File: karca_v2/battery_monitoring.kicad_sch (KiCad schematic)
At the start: 15 parts, among them U34 INA180A2, U36 TLV9301xDBV, U41 NUP4202, U42 MCP3204

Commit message: discrete traces
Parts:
- renumbered C59 to C73, C60 to C74, C61 to C75, C70 to C76, C71 to C77, R112 to R116, R113 to R117, R114 to R118, R115 to R119, U34 to U43, U42 to U44, U41 to U45, U36 to U46

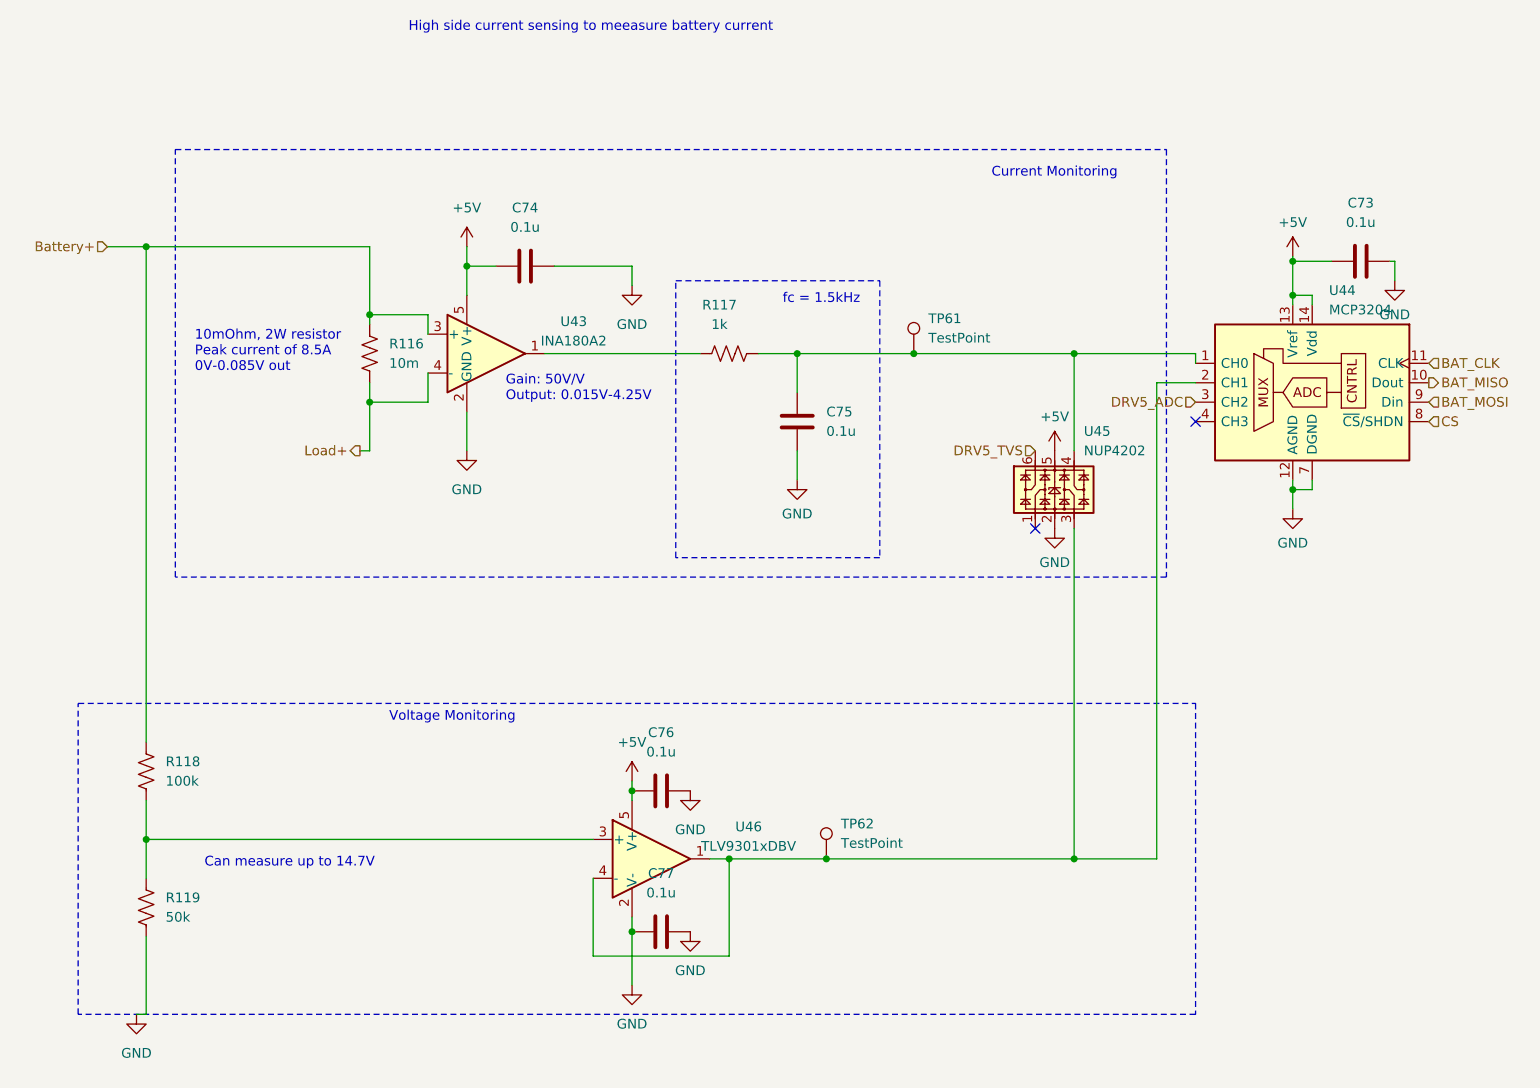
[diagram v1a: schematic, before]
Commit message: fixed TVS Diodes
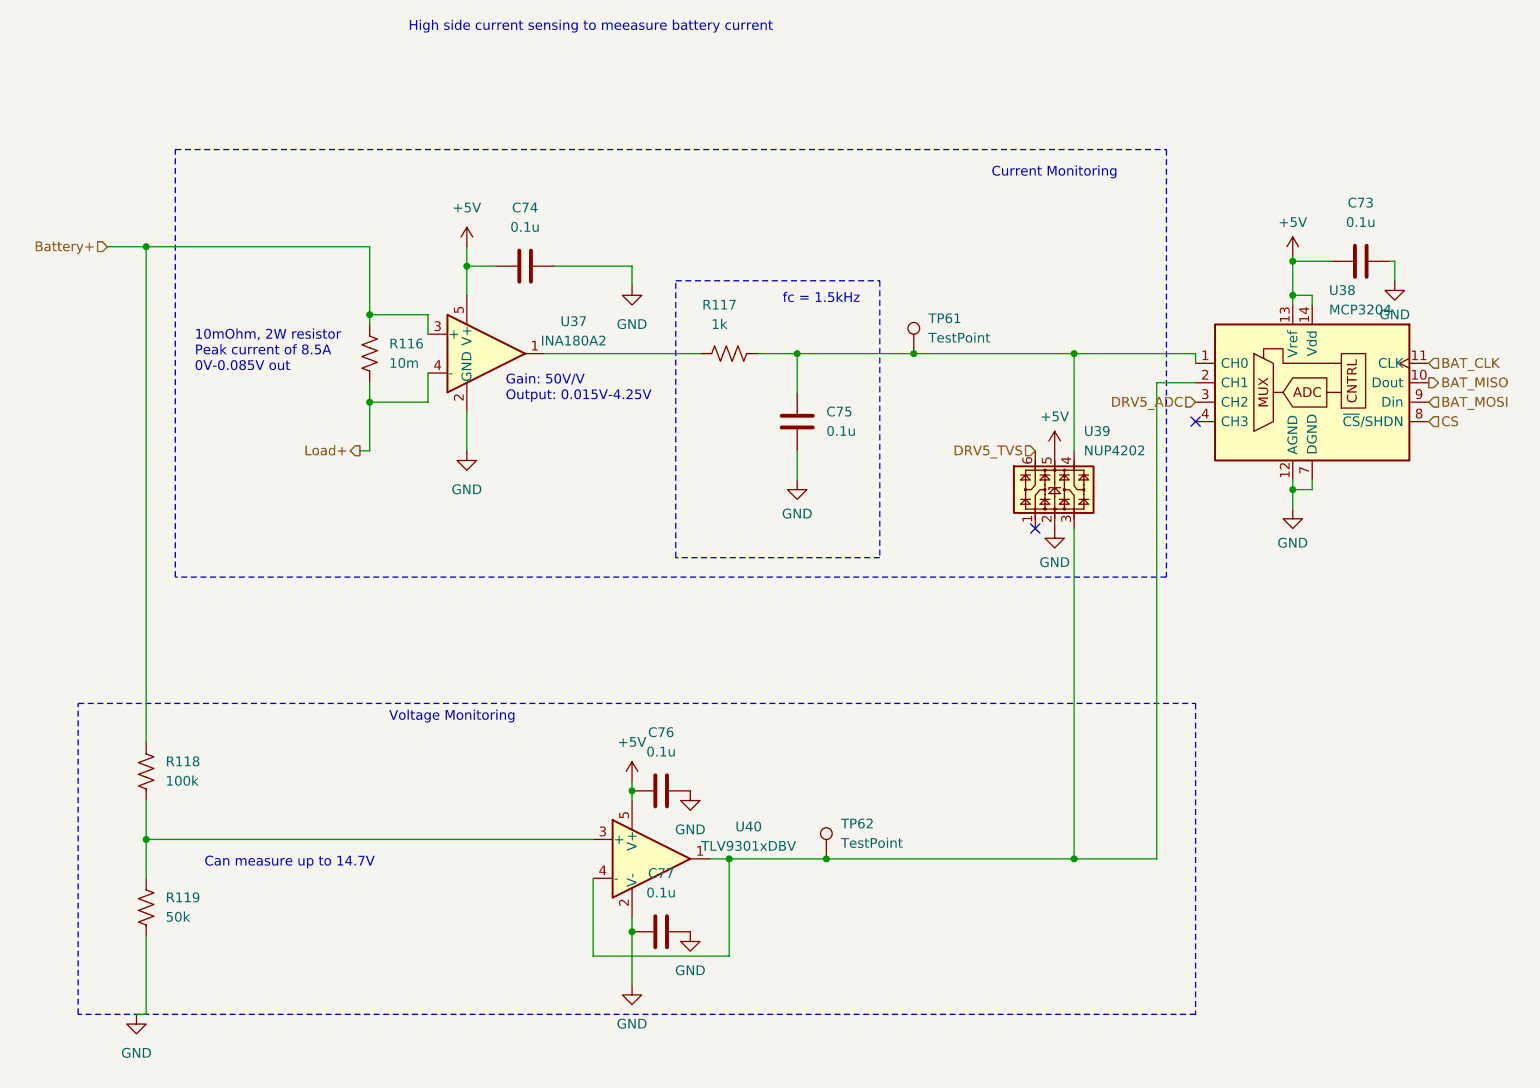
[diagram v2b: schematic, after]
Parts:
- renumbered U43 to U37, U44 to U38, U45 to U39, U46 to U40

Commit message: fixed violations
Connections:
- net BAT_CUR: now reaches C75.2, R117.2, TP61.1, U38.1 (CH0), U39.4
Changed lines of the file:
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@@
+    (effects (font (size 1.27 1.27)) (justify left bottom))
+  )
+  (label "BAT_CUR" (at 163.195 59.69 0) (fields_autoplaced)
     (effects (font (size 1.27 1.27)) (justify left bottom))
   )

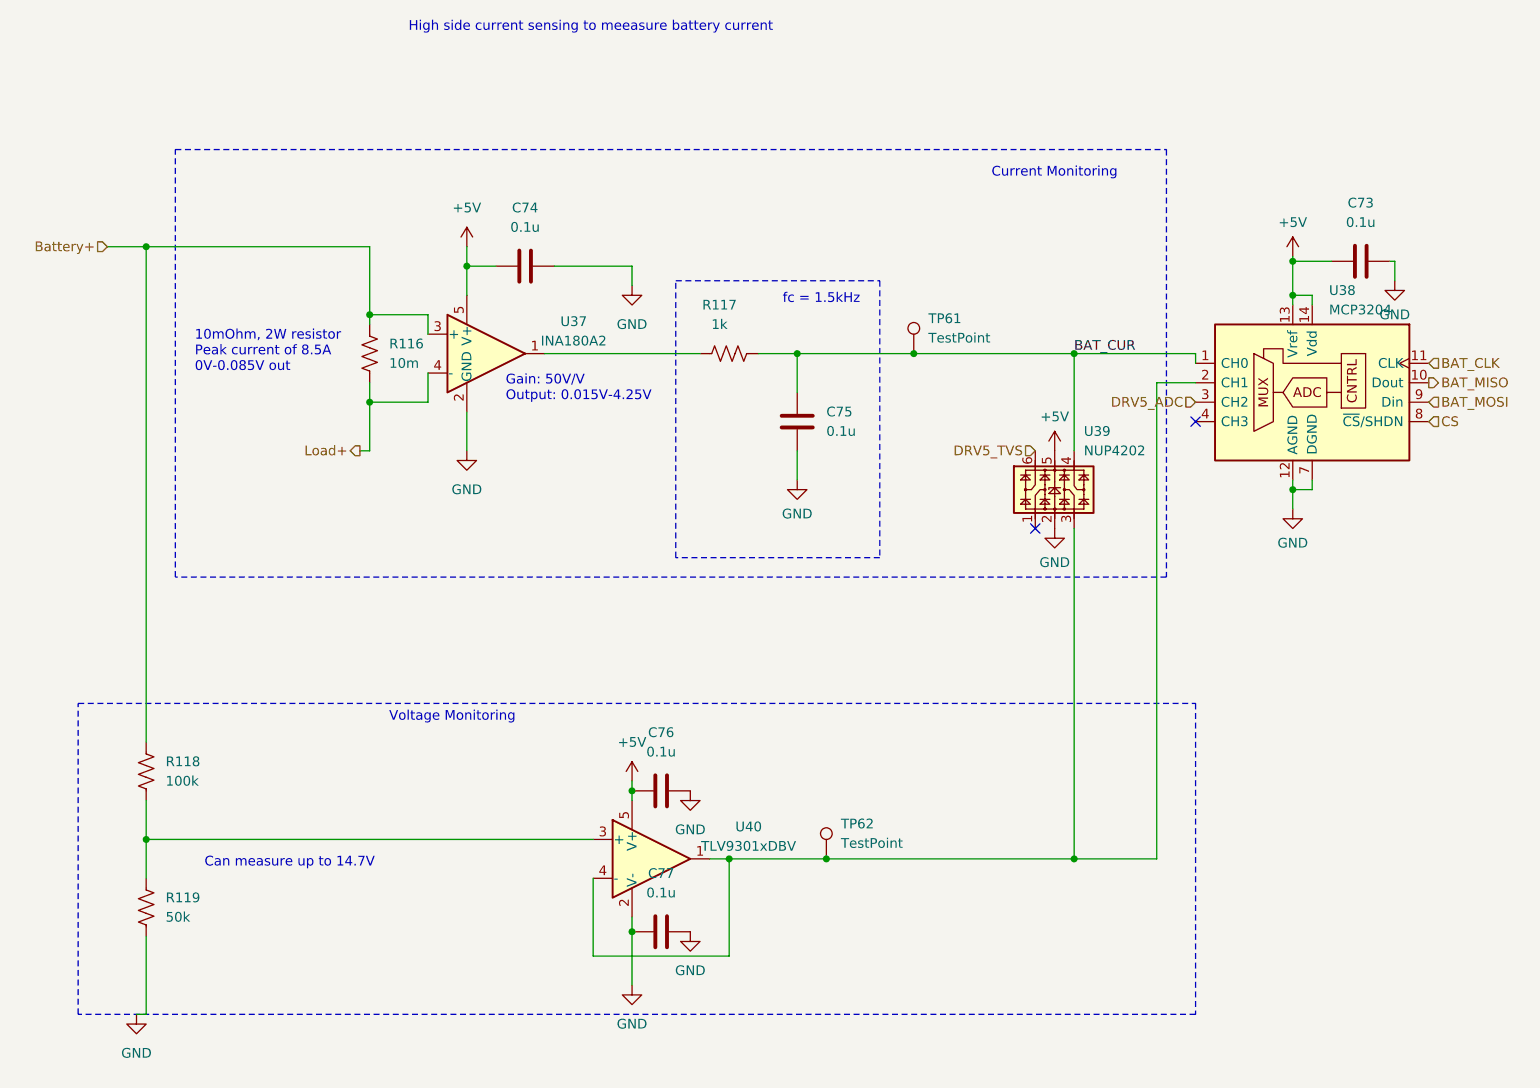
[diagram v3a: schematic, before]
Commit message: Fixed ground capacitors
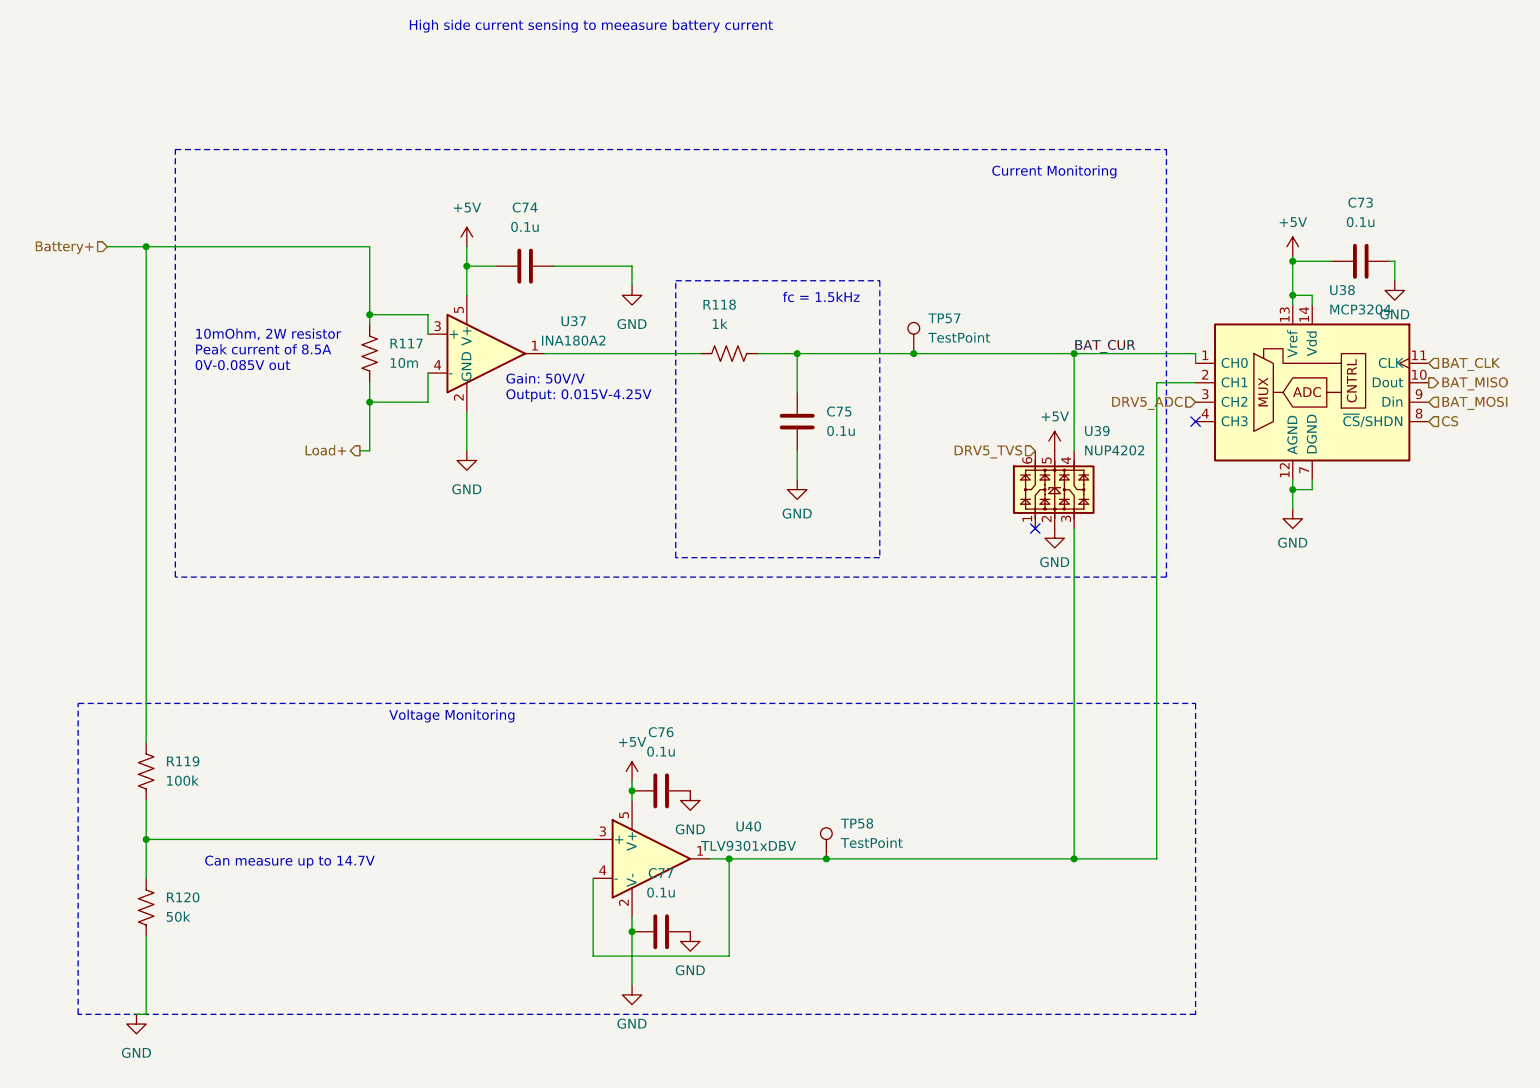
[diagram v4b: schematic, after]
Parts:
- renumbered R116 to R117, R117 to R118, R118 to R119, R119 to R120, TP61 to TP57, TP62 to TP58

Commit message: Passed all DRC, Added safety jumper to isolate regulators from rest of the board
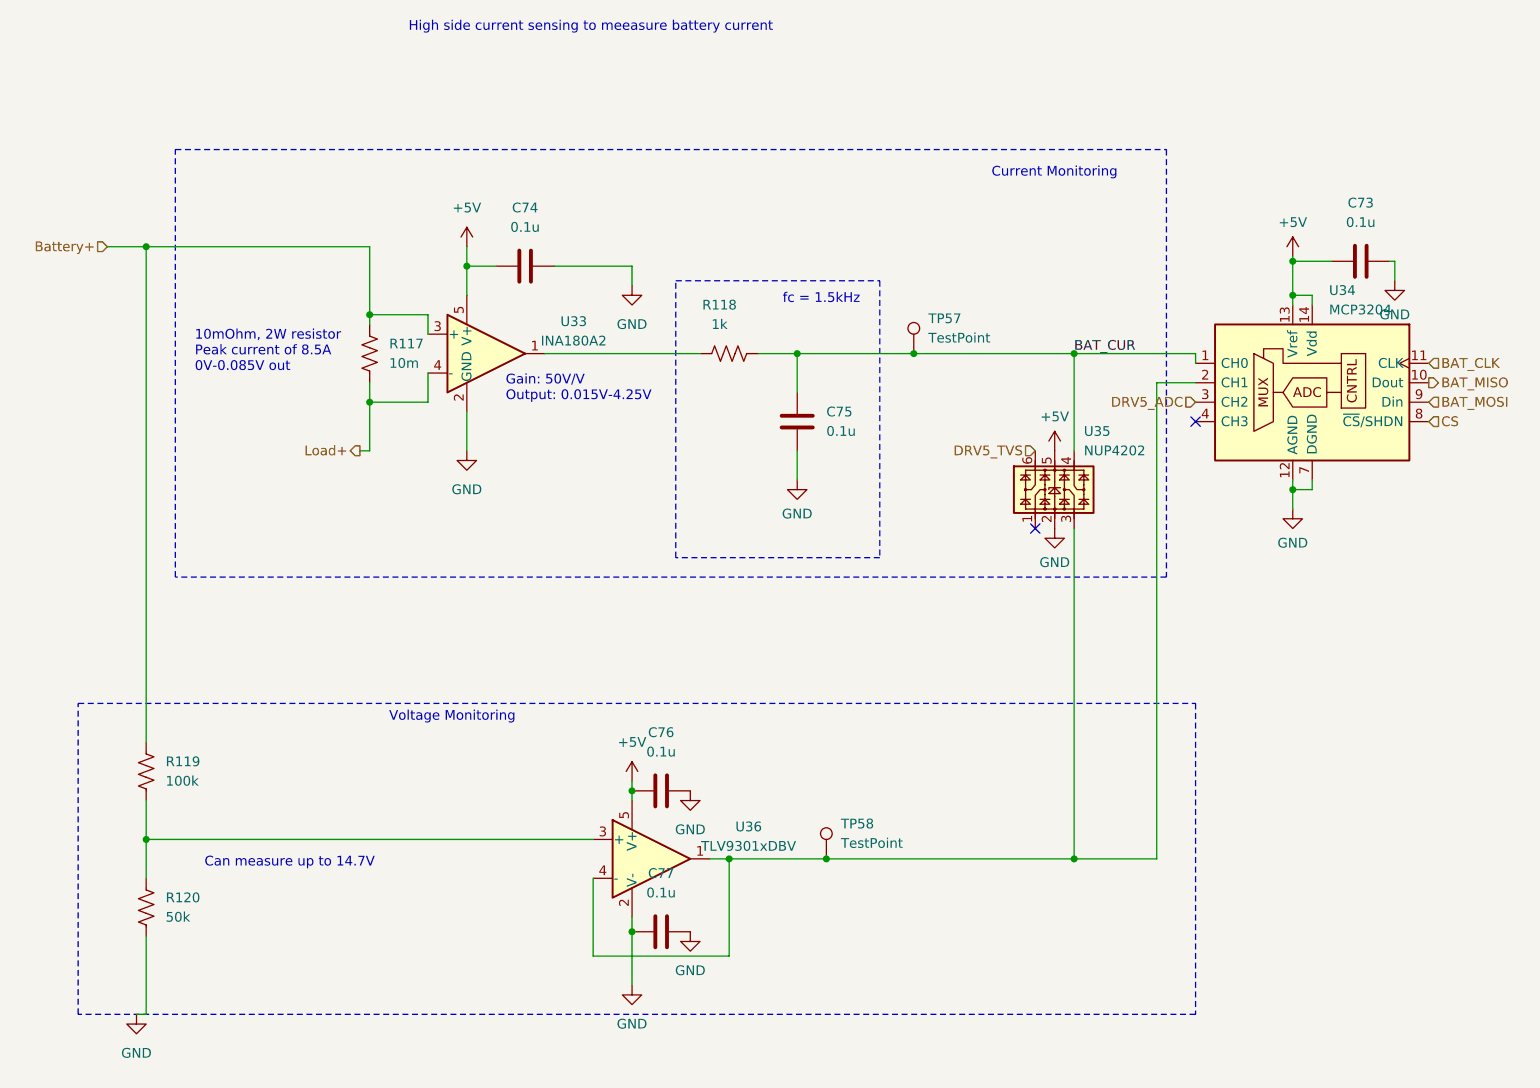
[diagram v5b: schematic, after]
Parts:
- renumbered U37 to U33, U38 to U34, U39 to U35, U40 to U36

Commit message: cleaned up documentation. Added production files and BOM. Marked Thermocouple components and THT components as DNP (excluded them from BOM too) to match version sent to JLCPCB for fabrication
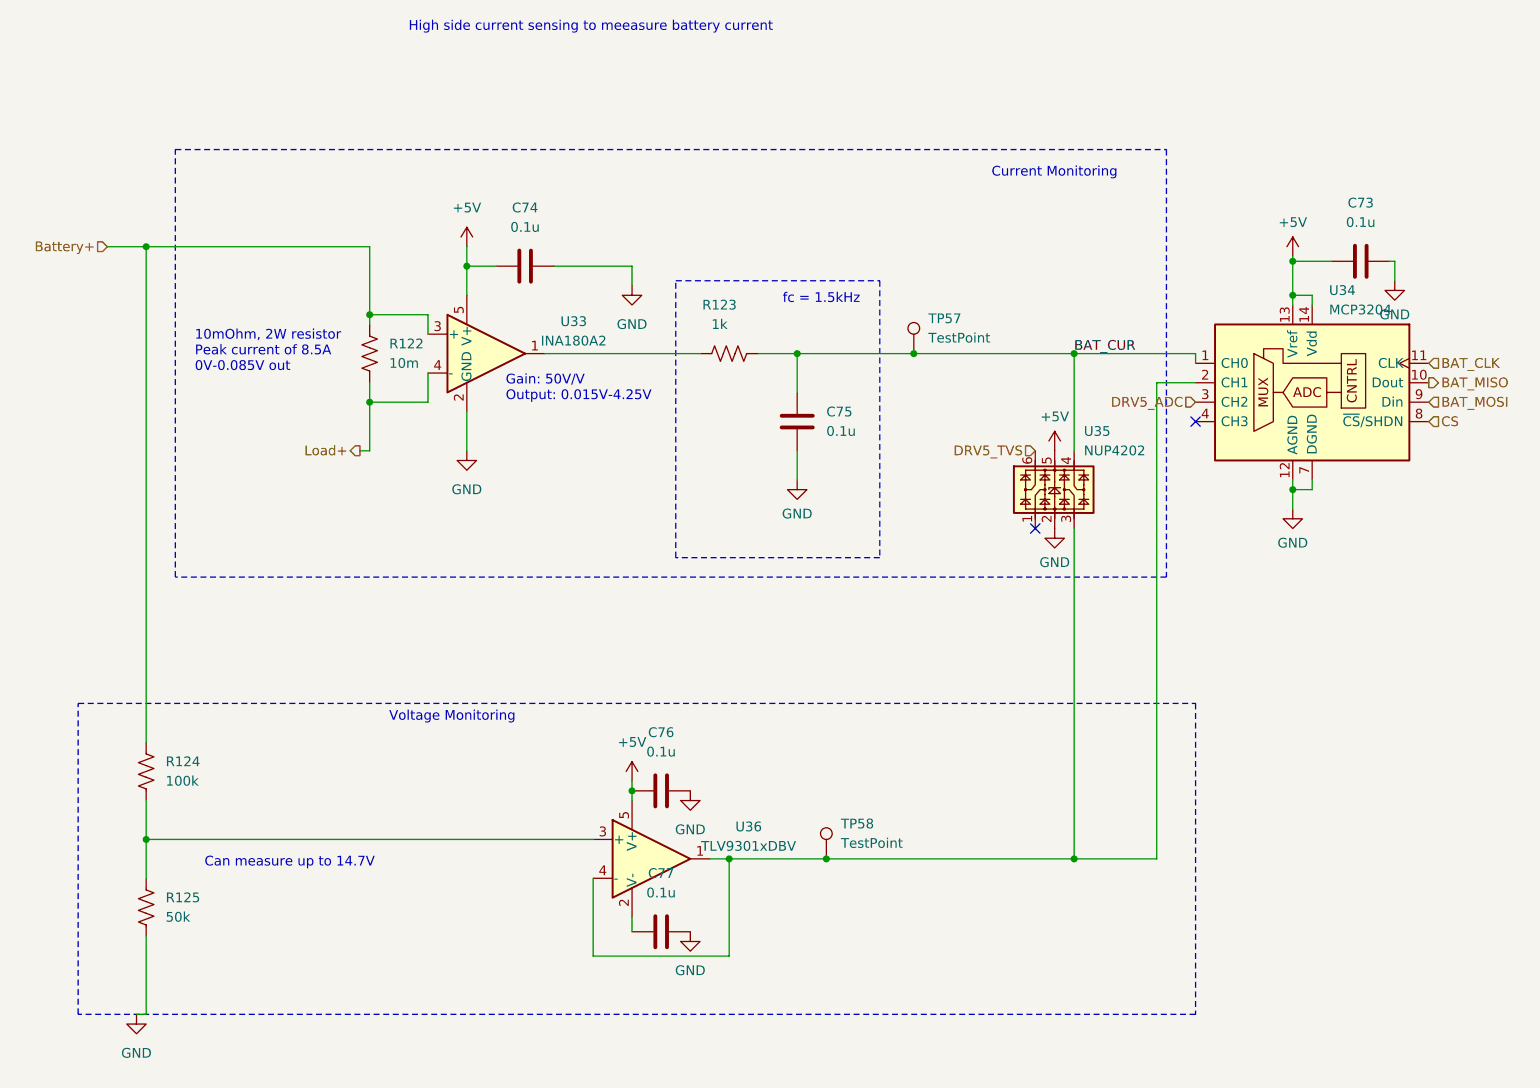
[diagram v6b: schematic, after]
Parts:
- R122: renamed from R117; footprint Resistor_SMD:R_1206_3216Metric -> Resistor_SMD:R_2512_6332Metric
- R125: renamed from R120; footprint Resistor_SMD:R_1206_3216Metric -> Resistor_SMD:R_0805_2012Metric
- renumbered R118 to R123, R119 to R124
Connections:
- net GND: no longer C77.1, U36.2 (V-)
- new net: C77.1, U36.2 (V-)
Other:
- company: (none) -> Rice Eclipse
- title: (none) -> kARCA 2.0 Engine Control System

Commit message: revisions for V2.1
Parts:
- removed C77: 0.1u, Capacitor_SMD:C_0402_1005Metric, symbol Device:C
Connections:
- net GND: now also U36.2 (V-)
